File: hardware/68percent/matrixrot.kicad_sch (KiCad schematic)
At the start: 37 parts

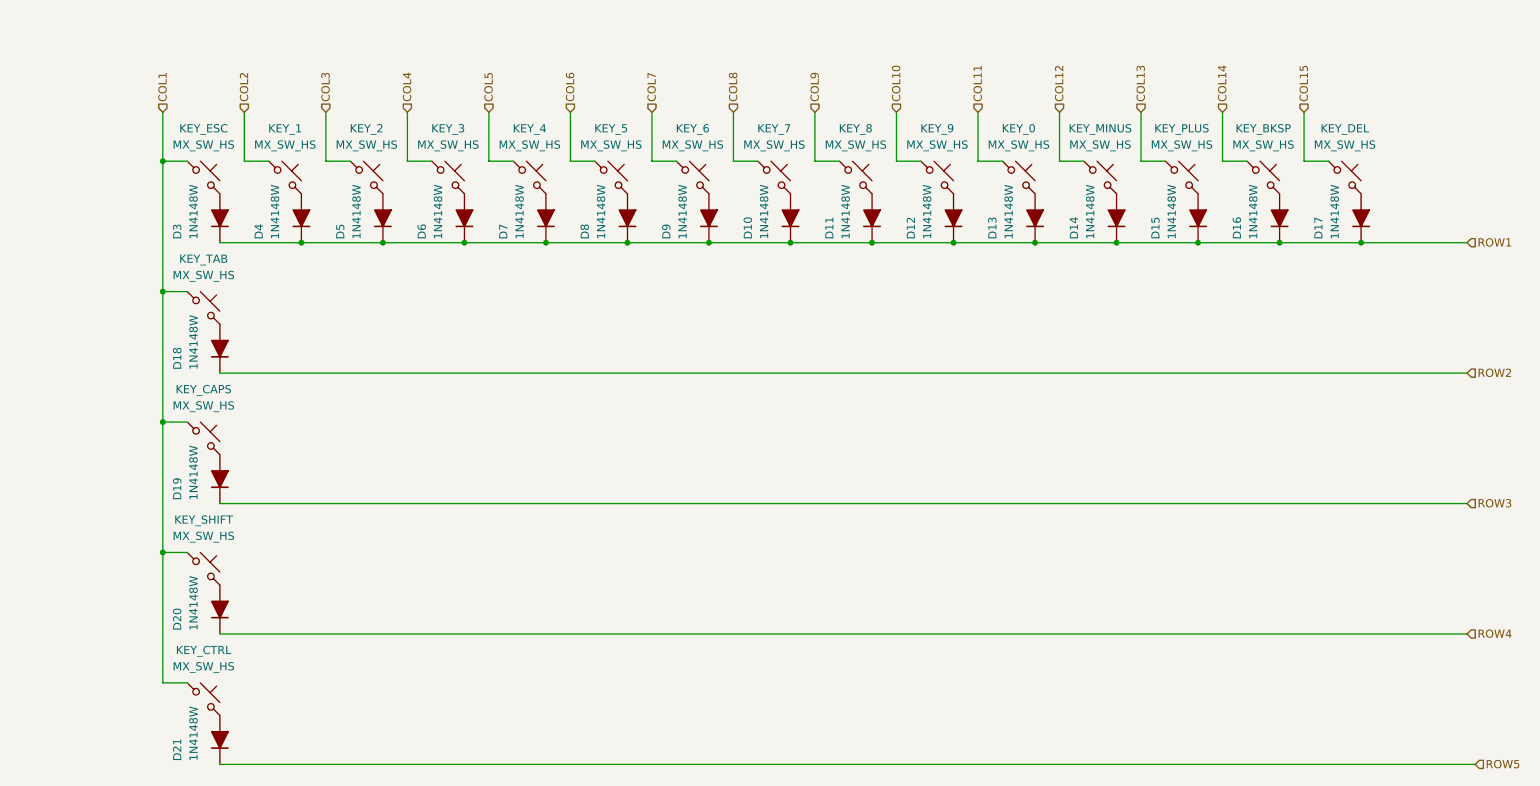
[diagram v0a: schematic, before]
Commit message: keyboardMatrix
finished the kbd matrix layout. subject to review. <3
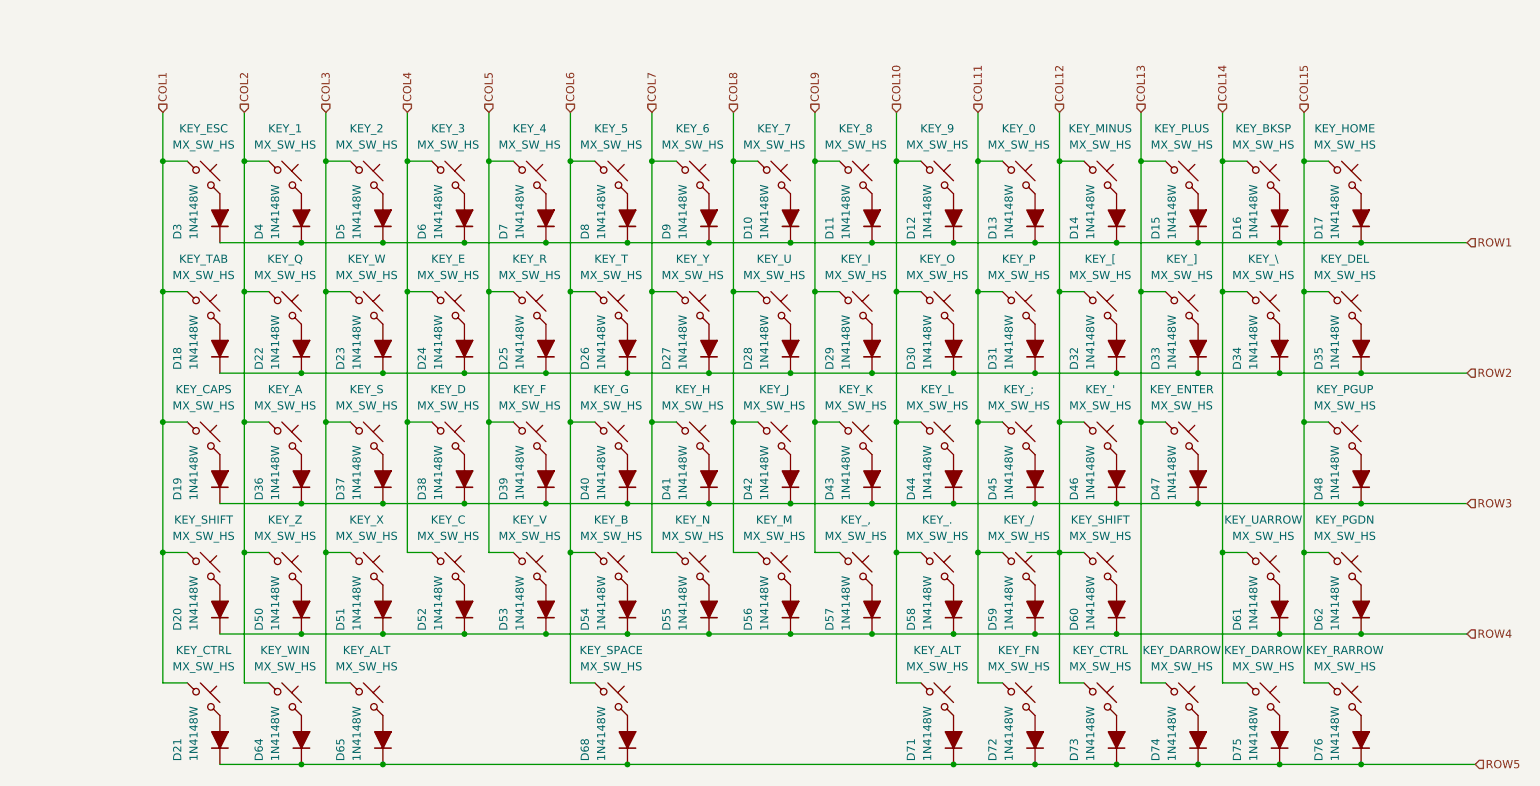
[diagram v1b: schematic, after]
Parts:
- added D22, D23, D24, D25, D26, D27, D28, D29, D30, D31, D32, D33, D34, D35, D36, D37, D38, D39, D40, D41, D42, D43, D44, D45, D46, D47, D48, D50, D51, D52, D53, D54, D55, D56, D57, D58, D59, D60, D61, D62, D64, D65, D68, D71, D72, D73, D74, D75, D76: 1N4148W, PCM_Diode_SMD_AKL:D_SOD-123, symbol PCM_Diode_AKL:1N4148W
- added KEY_', KEY_,, KEY_., KEY_/, KEY_3, KEY_;, KEY_A, KEY_ALT (x2), KEY_B, KEY_C, KEY_CTRL, KEY_D, KEY_DARROW, KEY_DEL, KEY_E, KEY_ENTER, KEY_F, KEY_FN, KEY_G, KEY_H, KEY_I, KEY_J, KEY_K, KEY_L, KEY_M, KEY_N, KEY_O, KEY_P, KEY_PGUP, KEY_Q, KEY_R, KEY_RARROW, KEY_S, KEY_SHIFT, KEY_SPACE, KEY_T, KEY_U, KEY_V, KEY_W, KEY_WIN, KEY_X, KEY_Y, KEY_Z: MX_SW_HS, PCM_marbastlib-mx:SW_MX_HS_CPG151101S11_1u, symbol PCM_marbastlib-mx:MX_SW_HS_CPG151101S11
- renumbered KEY_3 to KEY_1, KEY_DEL to KEY_HOME
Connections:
- net COL10: now also KEY_..1, KEY_ALT.1, KEY_L.1, KEY_O.1
- net COL11: now also KEY_/.1, KEY_;.1, KEY_FN.1, KEY_P.1
- net COL12: now also KEY_'.1, KEY_CTRL.1, KEY_SHIFT.1
- net COL13: now also KEY_DARROW.1, KEY_ENTER.1, KEY_SHIFT.1
- net COL14: now also KEY_DARROW.1, KEY_RARROW.1
- net COL15: now also KEY_DEL.1, KEY_PGUP.1, KEY_RARROW.1
- net COL2: now also KEY_A.1, KEY_Q.1, KEY_WIN.1, KEY_Z.1
- net COL3: now also KEY_ALT.1, KEY_S.1, KEY_W.1, KEY_X.1
- net COL4: now also KEY_3.1, KEY_C.1, KEY_D.1, KEY_E.1; no longer KEY_1.1
- net COL5: now also KEY_F.1, KEY_R.1, KEY_V.1
- net COL6: now also KEY_B.1, KEY_G.1, KEY_SPACE.1, KEY_T.1
- net COL7: now also KEY_H.1, KEY_N.1, KEY_Y.1
- net COL8: now also KEY_J.1, KEY_M.1, KEY_U.1
- net COL9: now also KEY_,.1, KEY_I.1, KEY_K.1
- net ROW2: now also D22.1 (K), D23.1 (K), D24.1 (K), D25.1 (K), D26.1 (K), D27.1 (K), D28.1 (K), D29.1 (K), D30.1 (K), D31.1 (K), D32.1 (K), D33.1 (K), D34.1 (K), D35.1 (K)
- net ROW3: now also D36.1 (K), D37.1 (K), D38.1 (K), D39.1 (K), D40.1 (K), D41.1 (K), D42.1 (K), D43.1 (K), D44.1 (K), D45.1 (K), D46.1 (K), D47.1 (K), D48.1 (K)
- net ROW4: now also D50.1 (K), D51.1 (K), D52.1 (K), D53.1 (K), D54.1 (K), D55.1 (K), D56.1 (K), D57.1 (K), D58.1 (K), D59.1 (K), D60.1 (K), D61.1 (K), D62.1 (K)
- net ROW5: now also D64.1 (K), D65.1 (K), D68.1 (K), D71.1 (K), D72.1 (K), D73.1 (K), D74.1 (K), D75.1 (K), D76.1 (K)
- net at KEY_1.2: now also D4.2 (A); no longer D6.2 (A)
- new net: D55.2 (A), KEY_N.2
- new net: D30.2 (A), KEY_O.2
- new net: D42.2 (A), KEY_J.2
- new net: D71.2 (A), KEY_ALT.2
- new net: D35.2 (A), KEY_DEL.2
- new net: D68.2 (A), KEY_SPACE.2
- new net: D36.2 (A), KEY_A.2
- new net: D65.2 (A), KEY_ALT.2
- new net: D27.2 (A), KEY_Y.2
- new net: D62.2 (A), KEY_RARROW.2
- new net: D34.2 (A), KEY_RARROW.2
- new net: D76.2 (A), KEY_RARROW.2
- new net: D52.2 (A), KEY_C.2
- new net: D60.2 (A), KEY_SHIFT.2
- new net: D28.2 (A), KEY_U.2
- new net: D32.2 (A), KEY_SHIFT.2
- new net: D74.2 (A), KEY_SHIFT.2
- new net: D72.2 (A), KEY_FN.2
- new net: D56.2 (A), KEY_M.2
- new net: D29.2 (A), KEY_I.2
- new net: D48.2 (A), KEY_PGUP.2
- new net: D53.2 (A), KEY_V.2
- new net: D24.2 (A), KEY_E.2
- new net: D47.2 (A), KEY_ENTER.2
- new net: D39.2 (A), KEY_F.2
- new net: D75.2 (A), KEY_DARROW.2
- new net: D61.2 (A), KEY_DARROW.2
- new net: D33.2 (A), KEY_DARROW.2
- new net: D26.2 (A), KEY_T.2
- new net: D73.2 (A), KEY_CTRL.2
- new net: D46.2 (A), KEY_'.2
- new net: D44.2 (A), KEY_L.2
- new net: D6.2 (A), KEY_3.2
- new net: D23.2 (A), KEY_W.2
- new net: D41.2 (A), KEY_H.2
- new net: D59.2 (A), KEY_/.2
- new net: D45.2 (A), KEY_;.2
- new net: D25.2 (A), KEY_R.2
- new net: D22.2 (A), KEY_Q.2
- new net: D58.2 (A), KEY_..2
- new net: D64.2 (A), KEY_WIN.2
- new net: D51.2 (A), KEY_X.2
- new net: D40.2 (A), KEY_G.2
- new net: D54.2 (A), KEY_B.2
- new net: D57.2 (A), KEY_,.2
- new net: D37.2 (A), KEY_S.2
- new net: D43.2 (A), KEY_K.2
- new net: D38.2 (A), KEY_D.2
- new net: D50.2 (A), KEY_Z.2
- new net: D31.2 (A), KEY_P.2

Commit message: pcb
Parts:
- added KEY_DARROW1, KEY_DARROW2, KEY_PGDN1, KEY_RARROW1, KEY_SHIFT2, KEY_UARROW1: MX_SW_HS, PCM_marbastlib-mx:SW_MX_HS_CPG151101S11_1u, symbol PCM_marbastlib-mx:MX_SW_HS_CPG151101S11
- renumbered KEY_' to KEY_'1, KEY_, to KEY_,1, KEY_. to KEY_.1, KEY_/ to KEY_/1, KEY_; to KEY_;1, KEY_A to KEY_A1, KEY_ALT to KEY_ALT1, KEY_ALT to KEY_ALT2, KEY_B to KEY_B1, KEY_BKSP to KEY_BKSP1, KEY_C to KEY_C1, KEY_CAPS to KEY_CAPS1, KEY_CTRL to KEY_CTRL1, KEY_CTRL to KEY_CTRL2, KEY_D to KEY_D1, KEY_DEL to KEY_DEL1, KEY_E to KEY_E1, KEY_ENTER to KEY_ENTER1, KEY_ESC to KEY_ESC1, KEY_F to KEY_F1, KEY_FN to KEY_FN1, KEY_G to KEY_G1, KEY_H to KEY_H1, KEY_HOME to KEY_HOME1, KEY_I to KEY_I1, KEY_J to KEY_J1, KEY_K to KEY_K1, KEY_L to KEY_L1, KEY_M to KEY_M1, KEY_MINUS to KEY_MINUS1, KEY_N to KEY_N1, KEY_O to KEY_O1, KEY_P to KEY_P1, KEY_PGUP to KEY_PGUP1, KEY_PLUS to KEY_PLUS1, KEY_Q to KEY_Q1, KEY_R to KEY_R1, KEY_S to KEY_S1, KEY_SHIFT to KEY_SHIFT1, KEY_SPACE to KEY_SPACE1, KEY_T to KEY_T1, KEY_TAB to KEY_TAB1, KEY_U to KEY_U1, KEY_V to KEY_V1, KEY_W to KEY_W1, KEY_WIN to KEY_WIN1, KEY_X to KEY_X1, KEY_Y to KEY_Y1, KEY_Z to KEY_Z1, KEY_SHIFT to KEY_[1, KEY_RARROW to KEY_\1, KEY_DARROW to KEY_]1
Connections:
- net COL12: now also KEY_SHIFT2.1
- net COL13: now also KEY_DARROW1.1; no longer KEY_[1.1
- net COL14: now also KEY_DARROW2.1, KEY_UARROW1.1; no longer KEY_]1.1
- net COL15: now also KEY_PGDN1.1, KEY_RARROW1.1; no longer KEY_\1.1
- net at KEY_\1.2: now also D34.2 (A); no longer D62.2 (A)
- net at D76.2 (A): now also KEY_RARROW1.2; no longer KEY_\1.2
- net at D60.2 (A): now also KEY_SHIFT2.2; no longer KEY_[1.2
- net at D74.2 (A): now also KEY_DARROW1.2; no longer KEY_[1.2
- net at KEY_]1.2: now also D33.2 (A); no longer D75.2 (A)
- net at D61.2 (A): now also KEY_UARROW1.2; no longer KEY_]1.2
- new net: D62.2 (A), KEY_PGDN1.2
- new net: D75.2 (A), KEY_DARROW2.2

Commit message: stuff stabs O
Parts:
- added S1: MX_stab, PCM_marbastlib-mx:STAB_MX_P_6.25u, symbol PCM_marbastlib-mx:MX_stab
- added S2: MX_stab, PCM_marbastlib-mx:STAB_MX_P_2.75u, symbol PCM_marbastlib-mx:MX_stab
- added S3, S5: MX_stab, PCM_marbastlib-mx:STAB_MX_P_2u, symbol PCM_marbastlib-mx:MX_stab
- added S4: MX_stab, PCM_marbastlib-mx:STAB_MX_P_2.25u, symbol PCM_marbastlib-mx:MX_stab

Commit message: 67
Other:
- moved on the sheet: S1, S2
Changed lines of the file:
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@@
 	(symbol
 		(lib_id "PCM_marbastlib-mx:MX_stab")
-		(at 139.7 137.16 0)
+		(at 38.1 119.38 0)
 		(unit 1)
 		(exclude_from_sim no)
@@
 		(fields_autoplaced yes)
 		(property "Reference" "S1"
-			(at 146.05 135.7629 0)
+			(at 44.45 117.9829 0)
 			(effects
 				(font
@@
 		)
 		(property "Value" "MX_stab"
-			(at 146.05 138.3029 0)
+			(at 44.45 120.5229 0)
 			(effects
 				(font
@@
 		)
 		(property "Footprint" "PCM_marbastlib-mx:STAB_MX_P_6.25u"
-			(at 139.7 137.16 0)
+			(at 38.1 119.38 0)
 			(effects
 				(font
@@
 		)
 		(property "Datasheet" ""
-			(at 139.7 137.16 0)
+			(at 38.1 119.38 0)
 			(effects
 				(font
@@
 		)
 		(property "Description" "Cherry MX-style stabilizer"
-			(at 139.7 137.16 0)
+			(at 38.1 119.38 0)
 			(effects
 				(font
@@
 	(symbol
 		(lib_id "PCM_marbastlib-mx:MX_stab")
-		(at 41.91 118.11 0)
+		(at 138.43 140.97 0)
 		(unit 1)
 		(exclude_from_sim no)
@@
 		(dnp no)
 		(property "Reference" "S2"
-			(at 35.56 119.2531 0)
+			(at 132.08 142.1131 0)
 			(effects
 				(font
@@
 		)
 		(property "Value" "MX_stab"
-			(at 35.56 116.7131 0)
+			(at 132.08 139.5731 0)
 			(effects
 				(font
@@
 		)
 		(property "Footprint" "PCM_marbastlib-mx:STAB_MX_P_2.75u"
-			(at 41.91 118.11 0)
+			(at 138.43 140.97 0)
 			(effects
 				(font
@@
 		)
 		(property "Datasheet" ""
-			(at 41.91 118.11 0)
+			(at 138.43 140.97 0)
 			(effects
 				(font
@@
 		)
 		(property "Description" "Cherry MX-style stabilizer"
-			(at 41.91 118.11 0)
+			(at 138.43 140.97 0)
 			(effects
 				(font

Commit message: layout adjustment
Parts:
- KEY_ALT1, KEY_CTRL1, KEY_SPACE1, KEY_WIN1: footprint PCM_marbastlib-mx:SW_MX_HS_CPG151101S11_1u -> PCM_Switch_Keyboard_Hotswap_Kailh:SW_Hotswap_Kailh_MX_Plated_1.25u
- KEY_SHIFT2: footprint PCM_marbastlib-mx:SW_MX_HS_CPG151101S11_1u -> PCM_Switch_Keyboard_Hotswap_Kailh:SW_Hotswap_Kailh_MX_Plated_1.75u
- KEY_\1: footprint PCM_marbastlib-mx:SW_MX_HS_CPG151101S11_1u -> PCM_marbastlib-mx:SW_MX_HS_CPG151101S11_1.5u
- S1: footprint PCM_marbastlib-mx:STAB_MX_P_6.25u -> PCM_marbastlib-mx:STAB_MX_2.25u
- S2: footprint PCM_marbastlib-mx:STAB_MX_P_2.75u -> PCM_marbastlib-mx:STAB_MX_P_6.25u
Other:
- moved on the sheet: S1, S2
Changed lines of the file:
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@@
 			)
 		)
-		(property "Footprint" "PCM_marbastlib-mx:SW_MX_HS_CPG151101S11_1u"
+		(property "Footprint" "PCM_Switch_Keyboard_Hotswap_Kailh:SW_Hotswap_Kailh_MX_Plated_1.25u"
 			(at 81.28 135.89 0)
 			(effects
@@
 			)
 		)
-		(property "Footprint" "PCM_marbastlib-mx:SW_MX_HS_CPG151101S11_1u"
+		(property "Footprint" "PCM_marbastlib-mx:SW_MX_HS_CPG151101S11_1.5u"
 			(at 220.98 74.93 0)
 			(effects
@@
 			)
 		)
-		(property "Footprint" "PCM_marbastlib-mx:SW_MX_HS_CPG151101S11_1u"
+		(property "Footprint" "PCM_Switch_Keyboard_Hotswap_Kailh:SW_Hotswap_Kailh_MX_Plated_1.75u"
 			(at 195.58 115.57 0)
 			(effects
@@
 			)
 		)
-		(property "Footprint" "PCM_marbastlib-mx:SW_MX_HS_CPG151101S11_1u"
+		(property "Footprint" "PCM_Switch_Keyboard_Hotswap_Kailh:SW_Hotswap_Kailh_MX_Plated_1.25u"
 			(at 55.88 135.89 0)
 			(effects
@@
 	)
 	(symbol
-		(lib_id "PCM_marbastlib-mx:MX_stab")
-		(at 208.28 115.57 0)
-		(unit 1)
-		(exclude_from_sim no)
-		(in_bom yes)
-		(on_board yes)
-		(dnp no)
-		(fields_autoplaced yes)
-		(property "Reference" "S3"
-			(at 214.63 114.1729 0)
-			(effects
-				(font
-					(size 1.27 1.27)
-				)
-				(justify left)
-			)
-		)
-		(property "Value" "MX_stab"
-			(at 214.63 116.7129 0)
-			(effects
-				(font
-					(size 1.27 1.27)
-				)
-				(justify left)
-			)
-		)
-		(property "Footprint" "PCM_marbastlib-mx:STAB_MX_P_2u"
-			(at 208.28 115.57 0)
-			(effects
-				(font
-					(size 1.27 1.27)
-				)
-				(hide yes)
-			)
-		)
-		(property "Datasheet" ""
-			(at 208.28 115.57 0)
-			(effects
-				(font
-					(size 1.27 1.27)
-				)
-				(hide yes)
-			)
-		)
-		(property "Description" "Cherry MX-style stabilizer"
-			(at 208.28 115.57 0)
-			(effects
-				(font
-					(size 1.27 1.27)
-				)
-				(hide yes)
-			)
-		)
-		(instances
-			(project ""
-				(path "/a3d0d559-cac8-4859-ad0f-79ad0c1a1a82/1d905906-6e74-4741-8b2e-53dc470a7c79"
-					(reference "S3")
-					(unit 1)
-				)
-			)
-		)
-	)
-	(symbol
 		(lib_id "PCM_marbastlib-mx:MX_SW_HS_CPG151101S11")
 		(at 68.58 54.61 0)
@@
 			)
 		)
-		(property "Footprint" "PCM_marbastlib-mx:SW_MX_HS_CPG151101S11_1u"
+		(property "Footprint" "PCM_Switch_Keyboard_Hotswap_Kailh:SW_Hotswap_Kailh_MX_Plated_1.25u"
 			(at 68.58 135.89 0)
 			(effects
@@
 	)
 	(symbol
+		(lib_id "PCM_marbastlib-mx:MX_stab")
+		(at 208.28 116.84 0)
+		(unit 1)
+		(exclude_from_sim no)
+		(in_bom yes)
+		(on_board yes)
+		(dnp no)
+		(property "Reference" "S3"
+			(at 206.756 109.22 0)
+			(effects
+				(font
+					(size 1.27 1.27)
+				)
+				(justify left)
+			)
+		)
+		(property "Value" "MX_stab"
+			(at 206.756 111.76 0)
+			(effects
+				(font
+					(size 1.27 1.27)
+				)
+				(justify left)
+			)
+		)
+		(property "Footprint" "PCM_marbastlib-mx:STAB_MX_P_2u"
+			(at 208.28 116.84 0)
+			(effects
+				(font
+					(size 1.27 1.27)
+				)
+				(hide yes)
+			)
+		)
+		(property "Datasheet" ""
+			(at 208.28 116.84 0)
+			(effects
+				(font
+					(size 1.27 1.27)
+				)
+				(hide yes)
+			)
+		)
+		(property "Description" "Cherry MX-style stabilizer"
+			(at 208.28 116.84 0)
+			(effects
+				(font
+					(size 1.27 1.27)
+				)
+				(hide yes)
+			)
+		)
+		(instances
+			(project "68percent"
+				(path "/a3d0d559-cac8-4859-ad0f-79ad0c1a1a82/1d905906-6e74-4741-8b2e-53dc470a7c79"
+					(reference "S3")
+					(unit 1)
+				)
+			)
+		)
+	)
+	(symbol
 		(lib_id "PCM_Diode_AKL:1N4148W")
 		(at 71.12 142.24 270)
@@
 	(symbol
 		(lib_id "PCM_marbastlib-mx:MX_stab")
-		(at 38.1 119.38 0)
+		(at 35.56 124.46 0)
 		(unit 1)
 		(exclude_from_sim no)
@@
 		(fields_autoplaced yes)
 		(property "Reference" "S1"
-			(at 44.45 117.9829 0)
+			(at 41.91 123.0629 0)
 			(effects
 				(font
@@
 		)
 		(property "Value" "MX_stab"
-			(at 44.45 120.5229 0)
+			(at 41.91 125.6029 0)
 			(effects
 				(font
@@
 			)
 		)
-		(property "Footprint" "PCM_marbastlib-mx:STAB_MX_P_6.25u"
-			(at 38.1 119.38 0)
+		(property "Footprint" "PCM_marbastlib-mx:STAB_MX_2.25u"
+			(at 35.56 124.46 0)
 			(effects
 				(font
@@
 		)
 		(property "Datasheet" ""
-			(at 38.1 119.38 0)
+			(at 35.56 124.46 0)
 			(effects
 				(font
@@
 		)
 		(property "Description" "Cherry MX-style stabilizer"
-			(at 38.1 119.38 0)
+			(at 35.56 124.46 0)
 			(effects
 				(font
@@
 			)
 		)
-		(property "Footprint" "PCM_marbastlib-mx:SW_MX_HS_CPG151101S11_1u"
+		(property "Footprint" "PCM_Switch_Keyboard_Hotswap_Kailh:SW_Hotswap_Kailh_MX_Plated_1.25u"
 			(at 119.38 135.89 0)
 			(effects
@@
 	(symbol
 		(lib_id "PCM_marbastlib-mx:MX_stab")
-		(at 138.43 140.97 0)
+		(at 146.05 139.7 0)
 		(unit 1)
 		(exclude_from_sim no)
@@
 		(dnp no)
 		(property "Reference" "S2"
-			(at 132.08 142.1131 0)
+			(at 139.7 140.8431 0)
 			(effects
 				(font
@@
 		)
 		(property "Value" "MX_stab"
-			(at 132.08 139.5731 0)
+			(at 139.7 138.3031 0)
 			(effects
 				(font
@@
 			)
 		)
-		(property "Footprint" "PCM_marbastlib-mx:STAB_MX_P_2.75u"
-			(at 138.43 140.97 0)
+		(property "Footprint" "PCM_marbastlib-mx:STAB_MX_P_6.25u"
+			(at 146.05 139.7 0)
 			(effects
 				(font
@@
 		)
 		(property "Datasheet" ""
-			(at 138.43 140.97 0)
+			(at 146.05 139.7 0)
 			(effects
 				(font
@@
 		)
 		(property "Description" "Cherry MX-style stabilizer"
-			(at 138.43 140.97 0)
+			(at 146.05 139.7 0)
 			(effects
 				(font

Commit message: pushy
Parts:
- D6: footprint PCM_Diode_SMD_AKL:D_SOD-123 -> PCM_Diode_THT_AKL:D_DO-35_SOD27_P7.62mm_Horizontal
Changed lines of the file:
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@@
 			)
 		)
-		(property "Footprint" "PCM_Diode_SMD_AKL:D_SOD-123"
+		(property "Footprint" "PCM_Diode_THT_AKL:D_DO-35_SOD27_P7.62mm_Horizontal"
 			(at 96.52 60.96 0)
 			(effects

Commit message: traces
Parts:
- D3: footprint PCM_Diode_SMD_AKL:D_SOD-123 -> PCM_4ms_Diode:D_DO-35_P7.62mm_Horizontal
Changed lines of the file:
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@@
 			)
 		)
-		(property "Footprint" "PCM_Diode_SMD_AKL:D_SOD-123"
+		(property "Footprint" "PCM_4ms_Diode:D_DO-35_P7.62mm_Horizontal"
 			(at 58.42 60.96 0)
 			(effects
